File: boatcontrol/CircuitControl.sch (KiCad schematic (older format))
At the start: 3 parts, among them SW4101 ESB30, SW4102 ESB30

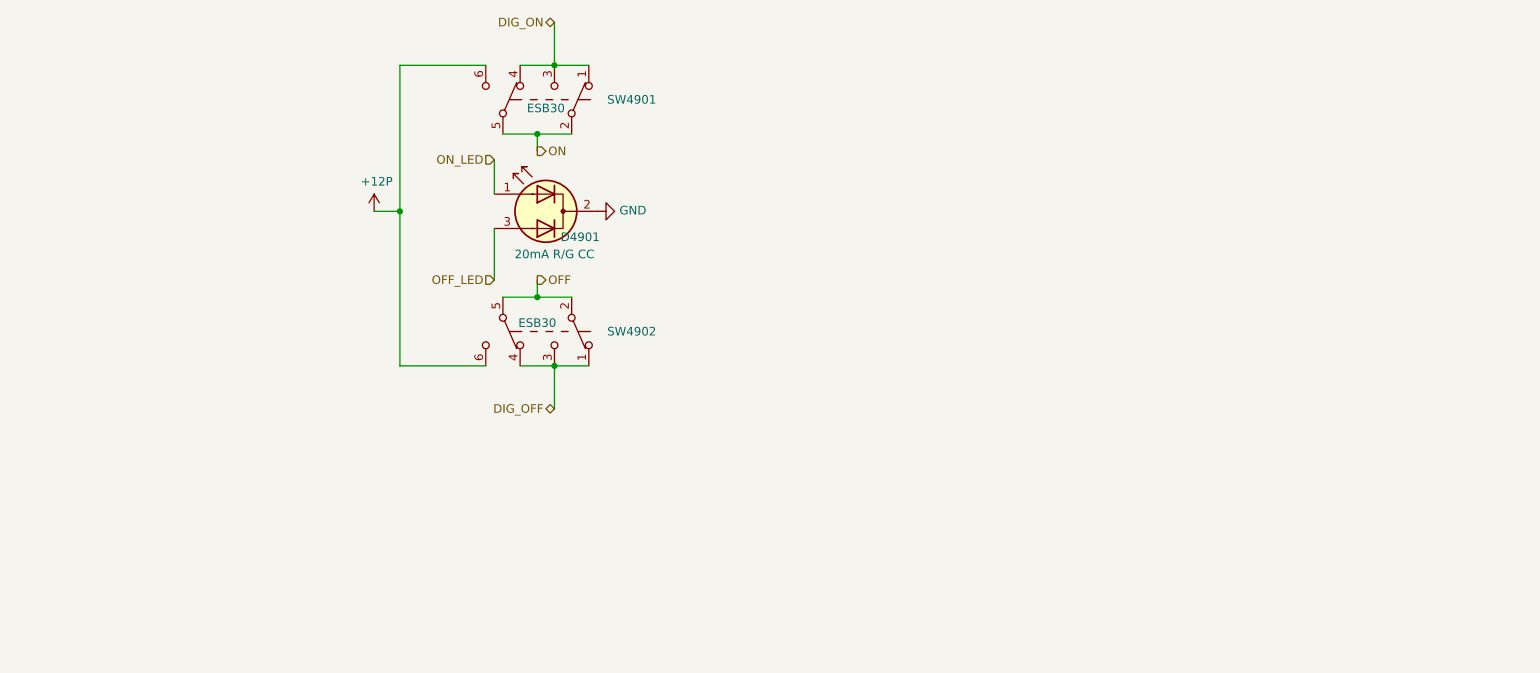
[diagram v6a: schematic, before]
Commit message: Fix switch layouts
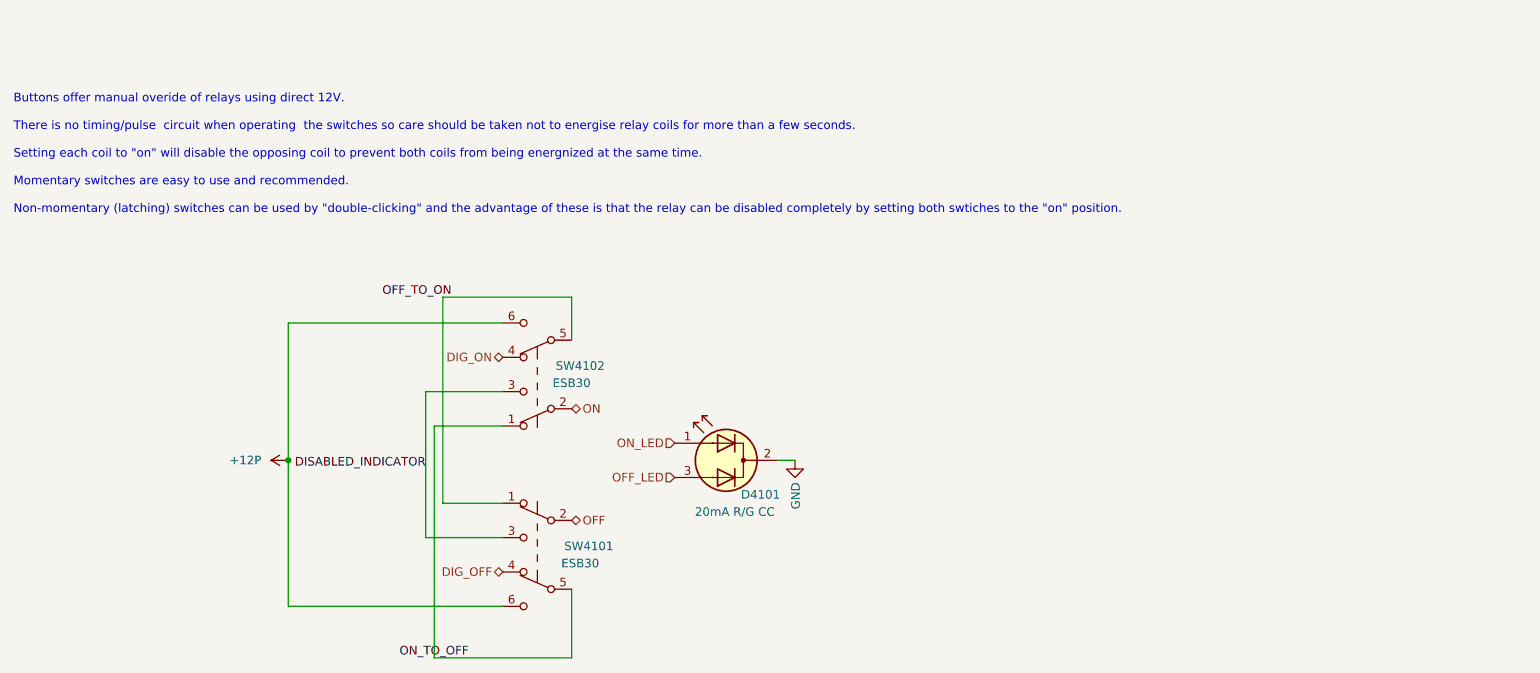
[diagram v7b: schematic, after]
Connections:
- net DIG_OFF: now also SW4101.4 (A); no longer SW4102.1 (A), SW4102.3 (C), SW4102.4 (A)
- net DIG_ON: now also SW4102.4 (A); no longer SW4101.1 (A), SW4101.3 (C), SW4101.4 (A)
- net OFF: now also SW4101.2 (B); no longer SW4102.2 (B), SW4102.5 (B)
- net ON: now also SW4102.2 (B); no longer SW4101.2 (B), SW4101.5 (B)
- new net DISABLED_INDICATOR: SW4101.3 (C), SW4102.3 (C)
- new net OFF_TO_ON: SW4101.1 (A), SW4102.5 (B)
- new net ON_TO_OFF: SW4101.5 (B), SW4102.1 (A)
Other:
- note added: "Buttons offer manual overide of relays using direct 12V.\n\nThere is no timing/pulse circuit when operating the switches so care should be taken not to energise relay coils for more than a few seconds.\n\nSetting each coil to "on" will disable the opposing coil to prevent both coils from being energnized at the same time.\n\nMomentary switches are easy to use and recommended.\n\nNon-momentary (la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"
- moved on the sheet: D4101, SW4101, SW4102
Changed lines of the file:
@@
 Comment4 ""
 $EndDescr
-Connection ~ 4950 3000
-Wire Wire Line
-	4950 2150 4950 3000
-Wire Wire Line
-	4950 3000 4950 3900
-Wire Wire Line
-	5950 3500 5750 3500
-Wire Wire Line
-	4950 2150 5450 2150
-Wire Wire Line
-	4950 3900 5450 3900
-Wire Wire Line
-	5550 2550 5750 2550
-Connection ~ 5850 2150
-Wire Wire Line
-	6050 2150 5850 2150
-Wire Wire Line
-	5650 2150 5850 2150
-Connection ~ 5850 3900
-Wire Wire Line
-	6050 3900 5850 3900
-Wire Wire Line
-	5650 3900 5850 3900
-Wire Wire Line
-	4800 3000 4950 3000
 $Comp
 L Switch:SW_Push_DPDT SW?
 U 1 1 E13B21A8
-P 5750 3700
+P 5750 3950
 AR Path="/E13B21A8" Ref="SW?"  Part="1"
 AR Path="/5FBFBEC9/E13B21A8" Ref="SW?"  Part="1"
@@
 AR Path="/E171B33C/E15855D9/E150D6D7/E13B21A8" Ref="SW4702"  Part="1"
 AR Path="/E171B33C/E15855D9/E150FD51/E13B21A8" Ref="SW4802"  Part="1"
-F 0 "SW4902" V 5750 4250 50  0000 C CNN
-F 1 " ESB30" V 5700 3700 50  0000 C CNN
-F 2 "BoatControl:SW_PUSH_ESB30_DPDT" H 5750 3900 50  0001 C CNN
-F 3 "https://www.mouser.ca/datasheet/2/315/sw_pu_eng_esb30-1511162.pdf" H 5750 3900 50  0001 C CNN
-	1    5750 3700
-	0    1    1    0
+F 0 "SW4102" H 5500 3900 50  0000 C CNN
+F 1 " ESB30" H 5550 4000 50  0000 C CNN
+F 2 "BoatControl:SW_PUSH_ESB30_DPDT" H 5750 4150 50  0001 C CNN
+F 3 "https://www.mouser.ca/datasheet/2/315/sw_pu_eng_esb30-1511162.pdf" H 5750 4150 50  0001 C CNN
+	1    5750 3950
+	-1   0    0    1
 $EndComp
 $Comp
 L power:+12P #PWR?
 U 1 1 E13B21AE
-P 4800 3000
+P 4300 4450
 AR Path="/5FBFBEC9/E13B21AE" Ref="#PWR?"  Part="1"
 AR Path="/768425E1/E13B21AE" Ref="#PWR?"  Part="1"
@@
 AR Path="/E171B33C/E15855D9/E150D6D7/E13B21AE" Ref="#PWR04701"  Part="1"
 AR Path="/E171B33C/E15855D9/E150FD51/E13B21AE" Ref="#PWR04801"  Part="1"
-F 0 "#PWR04901" H 4800 2850 50  0001 C CNN
-F 1 "+12P" H 4815 3173 50  0000 C CNN
-F 2 "" H 4800 3000 50  0001 C CNN
-F 3 "" H 4800 3000 50  0001 C CNN
-	1    4800 3000
-	1    0    0    -1
+F 0 "#PWR04101" H 4300 4300 50  0001 C CNN
+F 1 "+12P" V 4300 4700 50  0000 C CNN
+F 2 "" H 4300 4450 50  0001 C CNN
+F 3 "" H 4300 4450 50  0001 C CNN
+	1    4300 4450
+	0    -1   -1   0
 $EndComp
 $Comp
 L Switch:SW_Push_DPDT SW?
 U 1 1 E13B21B4
-P 5750 2350
+P 5750 5000
 AR Path="/E13B21B4" Ref="SW?"  Part="1"
 AR Path="/5FBFBEC9/E13B21B4" Ref="SW?"  Part="1"
@@
 AR Path="/E171B33C/E15855D9/E150D6D7/E13B21B4" Ref="SW4701"  Part="1"
 AR Path="/E171B33C/E15855D9/E150FD51/E13B21B4" Ref="SW4801"  Part="1"
-F 0 "SW4901" V 5750 2900 50  0000 C CNN
-F 1 " ESB30" V 5700 2400 50  0000 C CNN
-F 2 "BoatControl:SW_PUSH_ESB30_DPDT" H 5750 2550 50  0001 C CNN
-F 3 "https://www.mouser.ca/datasheet/2/315/sw_pu_eng_esb30-1511162.pdf" H 5750 2550 50  0001 C CNN
-	1    5750 2350
-	0    1    -1   0
+F 0 "SW4101" H 5450 5050 50  0000 C CNN
+F 1 " ESB30" H 5500 4950 50  0000 C CNN
+F 2 "BoatControl:SW_PUSH_ESB30_DPDT" H 5750 5200 50  0001 C CNN
+F 3 "https://www.mouser.ca/datasheet/2/315/sw_pu_eng_esb30-1511162.pdf" H 5750 5200 50  0001 C CNN
+	1    5750 5000
+	-1   0    0    -1
 $EndComp
-Wire Wire Line
-	5500 2900 5500 2700
-Wire Wire Line
-	5500 3100 5500 3400
 $Comp
 L Device:LED_Dual_ACA D?
 U 1 1 E13B21BC
-P 5800 3000
+P 6850 4450
 AR Path="/E13B21BC" Ref="D?"  Part="1"
 AR Path="/5FBFBEC9/E13B21BC" Ref="D?"  Part="1"
@@
 AR Path="/E171B33C/E15855D9/E150D6D7/E13B21BC" Ref="D4701"  Part="1"
 AR Path="/E171B33C/E15855D9/E150FD51/E13B21BC" Ref="D4801"  Part="1"
-F 0 "D4901" H 5600 2850 50  0000 C CNN
-F 1 "20mA R/G CC" H 5750 2750 50  0000 C CNN
-F 2 "LED_THT:LED_D5.0mm-3" H 5800 3000 50  0001 C CNN
-F 3 "http://www.kingbrightusa.com/images/catalog/SPEC/WP59EGW.pdf" H 5800 3000 50  0001 C CNN
-F 4 "WP59EGW" H 5800 3000 50  0001 C CNN "Model"
-F 5 "Kingbright" H 5800 3000 50  0001 C CNN "Manufacturer"
-	1    5800 3000
+F 0 "D4101" H 6650 4250 50  0000 C CNN
+F 1 "20mA R/G CC" H 6800 4150 50  0000 C CNN
+F 2 "LED_THT:LED_D5.0mm-3" H 6850 4450 50  0001 C CNN
+F 3 "http://www.kingbrightusa.com/images/catalog/SPEC/WP59EGW.pdf" H 6850 4450 50  0001 C CNN
+F 4 "WP59EGW" H 6850 4450 50  0001 C CNN "Model"
+F 5 "Kingbright" H 6850 4450 50  0001 C CNN "Manufacturer"
+	1    6850 4450
 	-1   0    0    -1
 $EndComp
-Text HLabel 5500 2700 0    50   Input ~ 0
-ON_LED
-Text HLabel 5500 3400 0    50   Input ~ 0
-OFF_LED
-Text HLabel 5850 1900 0    50   BiDi ~ 0
+Text HLabel 5550 3850 0    50   BiDi ~ 0
 DIG_ON
-Wire Wire Line
-	5850 1900 5850 2150
-Text HLabel 5850 4150 0    50   BiDi ~ 0
-DIG_OFF
-Wire Wire Line
-	5850 4150 5850 3900
-Text HLabel 5750 3400 2    50   Output ~ 0
-OFF
-Text HLabel 5750 2650 2    50   Output ~ 0
-ON
-Wire Wire Line
-	5750 2650 5750 2550
-Connection ~ 5750 2550
-Wire Wire Line
-	5750 2550 5950 2550
-Wire Wire Line
-	5750 3400 5750 3500
-Connection ~ 5750 3500
-Wire Wire Line
-	5750 3500 5550 3500
 $Comp
 L power:GND #PWR04102
 U 1 1 5F521E18
-P 6100 3000
+P 7250 4450
 AR Path="/E171B33C/E142CD30/E14BA326/5F521E18" Ref="#PWR04102"  Part="1"
 AR Path="/E171B33C/E142CD30/E150AEB9/5F521E18" Ref="#PWR04402"  Part="1"
@@
 AR Path="/E171B33C/E15855D9/E150D6D7/5F521E18" Ref="#PWR04702"  Part="1"
 AR Path="/E171B33C/E15855D9/E150FD51/5F521E18" Ref="#PWR04802"  Part="1"
-F 0 "#PWR04902" H 6100 2750 50  0001 C CNN
-F 1 "GND" V 6105 2872 50  0000 R CNN
-F 2 "" H 6100 3000 50  0001 C CNN
-F 3 "" H 6100 3000 50  0001 C CNN
-	1    6100 3000
-	0    -1   -1   0
+F 0 "#PWR04102" H 7250 4200 50  0001 C CNN
+F 1 "GND" V 7255 4322 50  0000 R CNN
+F 2 "" H 7250 4450 50  0001 C CNN
+F 3 "" H 7250 4450 50  0001 C CNN
+	1    7250 4450
+	1    0    0    -1
 $EndComp
+Text Notes 2700 3100 0    50   ~ 0
+Buttons offer manual overide of relays using direct 12V.\n\nThere is no timing/pulse  circuit when operating  the switches so care should be taken not to energise relay coils for more than a few seconds.\n\nSetting each coil to "on" will disable the opposing coil to prevent both coils from being energnized at the same time.\n\nMomentary switches are easy to use and recommended.\n\nNon-momentary (latching) switches can be used by "double-clicking" and the advantage of these is that the relay can be disabled completely by setting both swtiches to the "on" position.\n\n
+Text HLabel 6550 4350 0    50   Input ~ 0
+ON_LED
+Text HLabel 6550 4550 0    50   Input ~ 0
+OFF_LED
+Wire Wire Line
+	5950 5200 5950 5600
+Wire Wire Line
+	5950 3750 5950 3500
+Wire Wire Line
+	5550 4050 5100 4050
+Wire Wire Line
+	5100 4050 5100 4900
+Wire Wire Line
+	5100 4900 5550 4900
+Text Label 5100 4500 2    50   ~ 0
+DISABLED_INDICATOR
+Text Label 5250 3500 2    50   ~ 0
+OFF_TO_ON
+Text Label 5350 5600 2    50   ~ 0
+ON_TO_OFF
+Wire Wire Line
+	7150 4450 7250 4450
+Text HLabel 5550 5100 0    50   BiDi ~ 0
+DIG_OFF
+Text HLabel 5950 4800 2    50   BiDi ~ 0
+OFF
+Text HLabel 5950 4150 2    50   BiDi ~ 0
+ON
+Wire Wire Line
+	4300 5300 4300 4450
+Wire Wire Line
+	4300 3650 5550 3650
+Wire Wire Line
+	4300 5300 5550 5300
+Connection ~ 4300 4450
+Wire Wire Line
+	4300 4450 4300 3650
+Wire Wire Line
+	5200 3500 5200 4700
+Wire Wire Line
+	5150 5600 5150 4250
+Wire Wire Line
+	5150 5600 5950 5600
+Wire Wire Line
+	5150 4250 5550 4250
+Wire Wire Line
+	5200 3500 5950 3500
+Wire Wire Line
+	5200 4700 5550 4700
 $EndSCHEMATC

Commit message: Fix LED resistors
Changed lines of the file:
@@
 $Descr A4 11693 8268
 encoding utf-8
-Sheet 41 87
+Sheet 43 87
 Title "Boat Control Hat"
 Date "2020-07-09"
@@
 AR Path="/E171B33C/E15855D9/E150D6D7/E13B21A8" Ref="SW4702"  Part="1"
 AR Path="/E171B33C/E15855D9/E150FD51/E13B21A8" Ref="SW4802"  Part="1"
-F 0 "SW4102" H 5500 3900 50  0000 C CNN
+F 0 "SW4902" H 5500 3900 50  0000 C CNN
 F 1 " ESB30" H 5550 4000 50  0000 C CNN
 F 2 "BoatControl:SW_PUSH_ESB30_DPDT" H 5750 4150 50  0001 C CNN
@@
 AR Path="/E171B33C/E15855D9/E150D6D7/E13B21AE" Ref="#PWR04701"  Part="1"
 AR Path="/E171B33C/E15855D9/E150FD51/E13B21AE" Ref="#PWR04801"  Part="1"
-F 0 "#PWR04101" H 4300 4300 50  0001 C CNN
+F 0 "#PWR04901" H 4300 4300 50  0001 C CNN
 F 1 "+12P" V 4300 4700 50  0000 C CNN
 F 2 "" H 4300 4450 50  0001 C CNN
@@
 AR Path="/E171B33C/E15855D9/E150D6D7/E13B21B4" Ref="SW4701"  Part="1"
 AR Path="/E171B33C/E15855D9/E150FD51/E13B21B4" Ref="SW4801"  Part="1"
-F 0 "SW4101" H 5450 5050 50  0000 C CNN
+F 0 "SW4901" H 5450 5050 50  0000 C CNN
 F 1 " ESB30" H 5500 4950 50  0000 C CNN
 F 2 "BoatControl:SW_PUSH_ESB30_DPDT" H 5750 5200 50  0001 C CNN
@@
 AR Path="/E171B33C/E15855D9/E150D6D7/E13B21BC" Ref="D4701"  Part="1"
 AR Path="/E171B33C/E15855D9/E150FD51/E13B21BC" Ref="D4801"  Part="1"
-F 0 "D4101" H 6650 4250 50  0000 C CNN
+F 0 "D4901" H 6650 4250 50  0000 C CNN
 F 1 "20mA R/G CC" H 6800 4150 50  0000 C CNN
 F 2 "LED_THT:LED_D5.0mm-3" H 6850 4450 50  0001 C CNN
@@
 AR Path="/E171B33C/E15855D9/E150D6D7/5F521E18" Ref="#PWR04702"  Part="1"
 AR Path="/E171B33C/E15855D9/E150FD51/5F521E18" Ref="#PWR04802"  Part="1"
-F 0 "#PWR04102" H 7250 4200 50  0001 C CNN
+F 0 "#PWR04902" H 7250 4200 50  0001 C CNN
 F 1 "GND" V 7255 4322 50  0000 R CNN
 F 2 "" H 7250 4450 50  0001 C CNN
